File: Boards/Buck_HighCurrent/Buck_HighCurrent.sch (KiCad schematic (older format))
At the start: 25 parts, among them U1 TPS563231

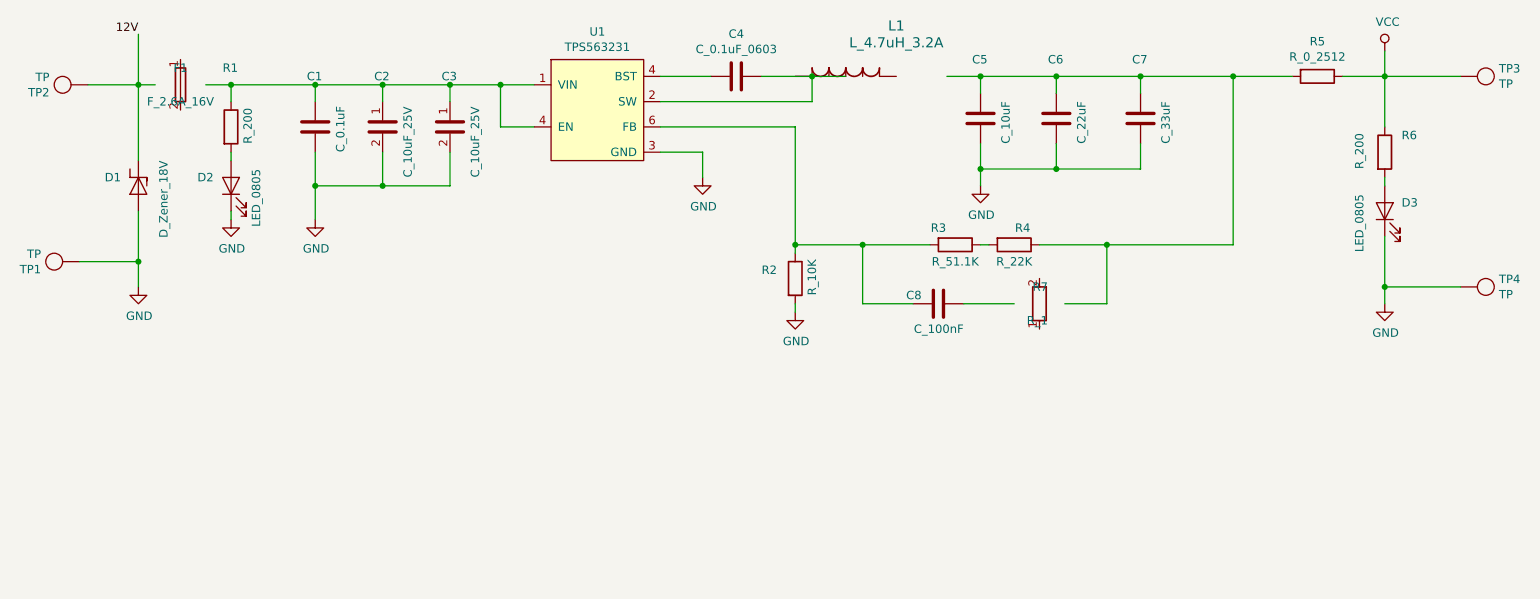
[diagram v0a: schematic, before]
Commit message: first pass layout with new buck.
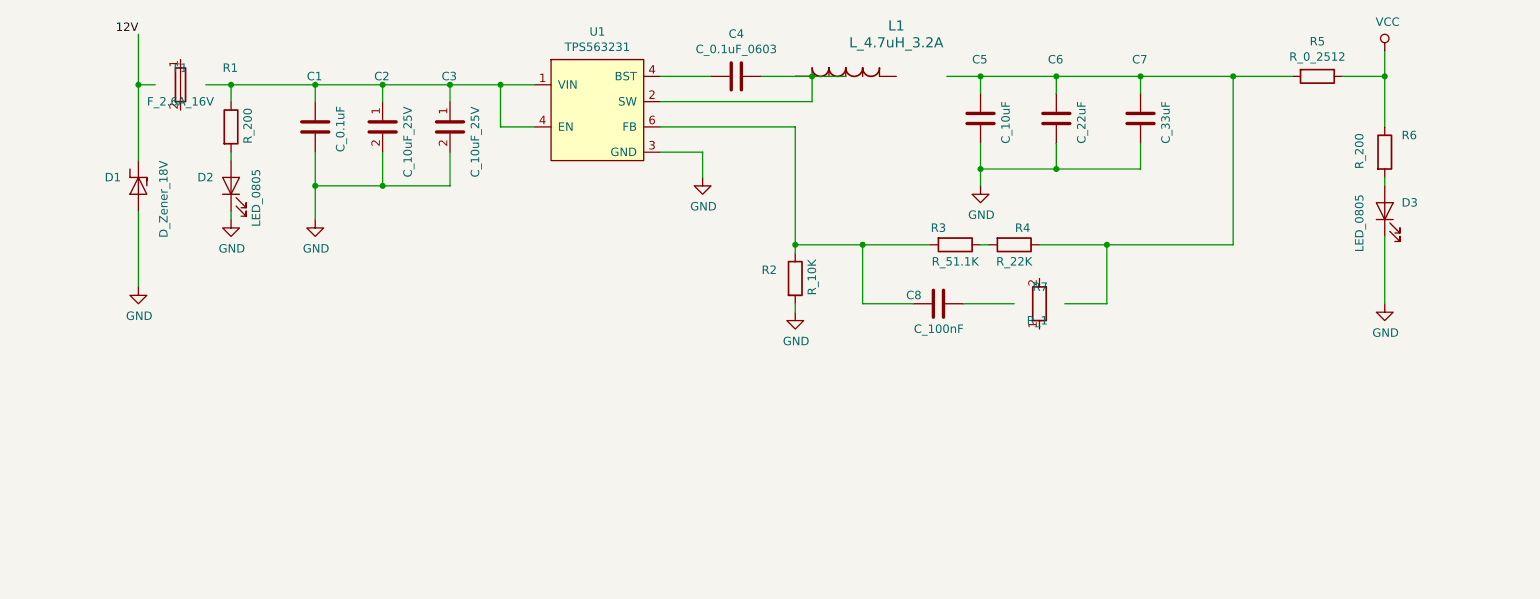
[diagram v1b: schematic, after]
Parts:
- removed TP1, TP2, TP3, TP4: TP, footprints:tp_1.6mm, symbol footprints:TP
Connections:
- wire segments 71 -> 65
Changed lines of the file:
@@
 	7300 3750 7000 3750
-$Comp
-L footprints:TP TP3
-U 1 1 5DDA5938
-P 10150 2400
-F 0 "TP3" V 10104 2428 50  0000 L CNN
-F 1 "TP" V 10195 2428 50  0000 L CNN
-F 2 "footprints:tp_1.6mm" H 10050 2300 50  0001 C CNN
-F 3 "http://www.keyelco.com/product-pdf.cfm?p=1314" H 10150 2400 50  0001 C CNN
-F 4 "DK" H 10250 2500 50  0001 C CNN "MFN"
-F 5 "36-5006-ND" H 10350 2600 50  0001 C CNN "MPN"
-F 6 "https://www.digikey.com/product-detail/en/keystone-electronics/5006/36-5006-ND/255330" H 10450 2700 50  0001 C CNN "PurchasingLink"
-	1    10150 2400
-	0    1    1    0
-$EndComp
-$Comp
-L footprints:TP TP4
-U 1 1 5DDA7C84
-P 10150 3650
-F 0 "TP4" V 10104 3678 50  0000 L CNN
-F 1 "TP" V 10195 3678 50  0000 L CNN
-F 2 "footprints:tp_1.6mm" H 10050 3550 50  0001 C CNN
-F 3 "http://www.keyelco.com/product-pdf.cfm?p=1314" H 10150 3650 50  0001 C CNN
-F 4 "DK" H 10250 3750 50  0001 C CNN "MFN"
-F 5 "36-5006-ND" H 10350 3850 50  0001 C CNN "MPN"
-F 6 "https://www.digikey.com/product-detail/en/keystone-electronics/5006/36-5006-ND/255330" H 10450 3950 50  0001 C CNN "PurchasingLink"
-	1    10150 3650
-	0    1    1    0
-$EndComp
-Wire Wire Line
-	9500 3350 9500 3650
-Wire Wire Line
-	9500 2400 9950 2400
-Wire Wire Line
-	9950 3650 9500 3650
-Connection ~ 9500 3650
-Wire Wire Line
-	9500 3650 9500 3750
-$Comp
-L footprints:TP TP1
-U 1 1 5DDB2371
-P 1550 3500
-F 0 "TP1" V 1504 3528 50  0000 L CNN
-F 1 "TP" V 1595 3528 50  0000 L CNN
-F 2 "footprints:tp_1.6mm" H 1450 3400 50  0001 C CNN
-F 3 "http://www.keyelco.com/product-pdf.cfm?p=1314" H 1550 3500 50  0001 C CNN
-F 4 "DK" H 1650 3600 50  0001 C CNN "MFN"
-F 5 "36-5006-ND" H 1750 3700 50  0001 C CNN "MPN"
-F 6 "https://www.digikey.com/product-detail/en/keystone-electronics/5006/36-5006-ND/255330" H 1850 3800 50  0001 C CNN "PurchasingLink"
-	1    1550 3500
-	0    -1   -1   0
-$EndComp
-Wire Wire Line
-	1750 3500 2100 3500
-Wire Wire Line
-	2100 3200 2100 3500
-Connection ~ 2100 3500
-Wire Wire Line
-	2100 3500 2100 3650
-$Comp
-L footprints:TP TP2
-U 1 1 5DDB56F7
-P 1600 2450
-F 0 "TP2" V 1554 2478 50  0000 L CNN
-F 1 "TP" V 1645 2478 50  0000 L CNN
-F 2 "footprints:tp_1.6mm" H 1500 2350 50  0001 C CNN
-F 3 "http://www.keyelco.com/product-pdf.cfm?p=1314" H 1600 2450 50  0001 C CNN
-F 4 "DK" H 1700 2550 50  0001 C CNN "MFN"
-F 5 "36-5006-ND" H 1800 2650 50  0001 C CNN "MPN"
-F 6 "https://www.digikey.com/product-detail/en/keystone-electronics/5006/36-5006-ND/255330" H 1900 2750 50  0001 C CNN "PurchasingLink"
-	1    1600 2450
-	0    -1   -1   0
-$EndComp
-Wire Wire Line
-	1800 2450 2100 2450
 $Comp
 L footprints:R_10K R2
@@
 Wire Wire Line
 	7850 3400 8600 3400
+Wire Wire Line
+	2100 3200 2100 3650
+Wire Wire Line
+	9500 3350 9500 3750
 $EndSCHEMATC

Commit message: 3A buck, rev2.0, no magic smoke now
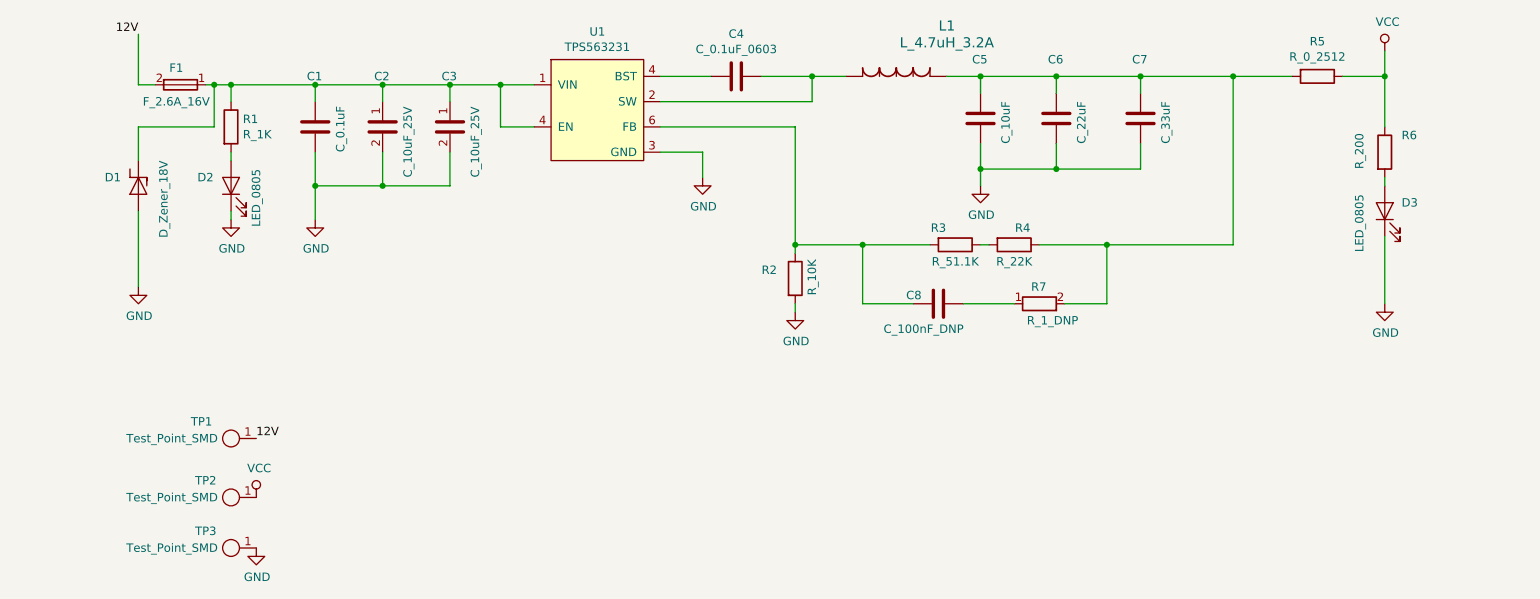
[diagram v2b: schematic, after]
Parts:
- removed R1: R_200, footprints:R_0805_OEM, symbol footprints:R_200
- added R1: R_1K, footprints:R_0805_OEM, symbol footprints:R_1K
- added TP1, TP2, TP3: Test_Point_SMD, footprints:Test_Point_SMD, symbol formula:Test_Point_SMD
- C8: value C_100nF -> C_100nF_DNP
- R7: value R_1 -> R_1_DNP
- U1: footprint footprints:SOT-563 -> Package_TO_SOT_SMD:SOT-563
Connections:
- wire segments 65 -> 68
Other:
- moved on the sheet: F1, L1, R7
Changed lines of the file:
@@
-$EndComp
-$Comp
-L footprints:R_200 R1
-U 1 1 5DD24939
-P 2650 2700
-F 0 "R1" H 2600 3050 50  0000 L CNN
-F 1 "R_200" V 2750 2600 50  0000 L CNN
-F 2 "footprints:R_0805_OEM" H 2580 2700 50  0001 C CNN
-F 3 "https://www.seielect.com/Catalog/SEI-RMCF_RMCP.pdf" H 2730 2700 50  0001 C CNN
-F 4 "DK" H 2650 2700 60  0001 C CNN "MFN"
-F 5 "RMCF0805JT200RCT-ND" H 2650 2700 60  0001 C CNN "MPN"
-F 6 "https://www.digikey.com/products/en?keywords=RMCF0805JT200RCT-ND" H 3130 3100 60  0001 C CNN "PurchasingLink"
-	1    2650 2700
-	1    0    0    -1
 $EndComp
 $Comp
@@
 	1    0    0    -1
 $EndComp
-Wire Wire Line
-	2100 2900 2100 2450
 $Comp
 L footprints:F_2.6A_16V F1
 U 1 1 5DD2DCBD
 P 2350 2450
-F 0 "F1" V 2250 2450 50  0000 C CNN
-F 1 "F_2.6A_16V" V 2450 2450 50  0000 C CNN
+F 0 "F1" H 2375 2350 50  0000 C CNN
+F 1 "F_2.6A_16V" H 2375 2550 50  0000 C CNN
 F 2 "Fuse:Fuse_1812_4532Metric" H 2350 2450 50  0001 C CNN
 F 3 "https://www.belfuse.com/resources/CircuitProtection/datasheets/0ZCG%20Nov2016.pdf" H 2350 2450 50  0001 C CNN
 F 4 "https://www.digikey.com/product-detail/en/bel-fuse-inc/0ZCG0260BF2B/507-1780-6-ND/4156287" H 2410 2359 50  0001 L CNN "Digikey"
 	1    2350 2450
-	0    1    1    0
+	-1   0    0    1
 $EndComp
 Wire Wire Line
@@
 Connection ~ 4250 2450
 Wire Wire Line
-	2500 2450 2650 2450
+	2500 2450 2550 2450
 Connection ~ 2650 2450
 Wire Wire Line
@@
 L footprints:IHLP2020BZER4R7M11 L1
 U 1 1 5DD494D5
-P 6300 2400
-F 0 "L1" H 6600 2700 60  0000 C CNN
-F 1 "L_4.7uH_3.2A" H 6600 2600 60  0000 C CNN
-F 2 "footprints:IHLP2020BZER4R7M11" H 6575 2115 60  0001 C CNN
-F 3 "http://www.vishay.com/docs/34261/ihlp2020bz11.pdf" H 6300 2400 60  0001 C CNN
-F 4 "https://www.digikey.com/product-detail/en/vishay-dale/IHLP2020BZER4R7M11/541-1222-1-ND/2025112" H 6300 2400 50  0001 C CNN "Vendor Link"
-	1    6300 2400
+P 6600 2400
+F 0 "L1" H 6900 2700 60  0000 C CNN
+F 1 "L_4.7uH_3.2A" H 6900 2600 60  0000 C CNN
+F 2 "footprints:IHLP2020BZER4R7M11" H 6875 2115 60  0001 C CNN
+F 3 "http://www.vishay.com/docs/34261/ihlp2020bz11.pdf" H 6600 2400 60  0001 C CNN
+F 4 "https://www.digikey.com/product-detail/en/vishay-dale/IHLP2020BZER4R7M11/541-1222-1-ND/2025112" H 6600 2400 50  0001 C CNN "Vendor Link"
+	1    6600 2400
 	1    0    0    -1
 $EndComp
@@
 Wire Wire Line
 	2100 2150 2100 2450
-Connection ~ 2100 2450
 Wire Wire Line
 	7450 3400 7850 3400
@@
 P 6850 3750
 F 0 "C8" V 6900 3850 50  0000 L CNN
-F 1 "C_100nF" V 6700 3600 50  0000 L CNN
+F 1 "C_100nF_DNP" V 6700 3600 50  0000 L CNN
 F 2 "footprints:C_0603_1608Metric" H 6888 3600 50  0001 C CNN
 F 3 "http://www.samsungsem.com/kr/support/product-search/mlcc/CL10A475KQ8NNNC.jsp" H 6875 3850 50  0001 C CNN
@@
 U 1 1 5DD86588
 P 7450 3750
-F 0 "R7" V 7550 3700 50  0000 L CNN
-F 1 "R_1" V 7350 3700 50  0000 L CNN
+F 0 "R7" H 7400 3850 50  0000 L CNN
+F 1 "R_1_DNP" H 7375 3650 50  0000 L CNN
 F 2 "footprints:R_0603_1608Metric" H 7450 3750 50  0001 C CNN
 F 3 "" H 7450 3750 50  0001 C CNN
 F 4 "https://www.digikey.com/product-detail/en/yageo/RC0603FR-071RL/311-1.00HRCT-ND/729789" H 7450 3750 50  0001 C CNN "Link"
 	1    7450 3750
-	0    -1   -1   0
+	1    0    0    -1
 $EndComp
 $Comp
@@
 F 0 "U1" H 4825 3665 50  0000 C CNN
 F 1 "TPS563231" H 4825 3574 50  0000 C CNN
-F 2 "footprints:SOT-563" H 4850 3050 50  0001 C CNN
+F 2 "Package_TO_SOT_SMD:SOT-563" H 4850 3050 50  0001 C CNN
 F 3 "" H 4850 3050 50  0001 C CNN
 	1    4850 2900
@@
 Wire Wire Line
 	9500 3350 9500 3750
+Wire Wire Line
+	2100 2900 2100 2700
+Wire Wire Line
+	2100 2700 2550 2700
+Wire Wire Line
+	2550 2700 2550 2450
+Connection ~ 2550 2450
+Wire Wire Line
+	2550 2450 2650 2450
+$Comp
+L formula:Test_Point_SMD TP1
+U 1 1 5E474401
+P 2750 4550
+F 0 "TP1" V 2850 4825 50  0000 C CNN
+F 1 "Test_Point_SMD" V 2750 5000 50  0000 C CNN
+F 2 "footprints:Test_Point_SMD" H 2750 4400 50  0001 C CNN
+F 3 "" H 2750 4550 50  0001 C CNN
+	1    2750 4550
+	0    -1   -1   0
+$EndComp
+$Comp
+L formula:Test_Point_SMD TP2
+U 1 1 5E475044
+P 2750 4900
+F 0 "TP2" V 2850 5150 50  0000 C CNN
+F 1 "Test_Point_SMD" V 2750 5350 50  0000 C CNN
+F 2 "footprints:Test_Point_SMD" H 2750 4750 50  0001 C CNN
+F 3 "" H 2750 4900 50  0001 C CNN
+	1    2750 4900
+	0    -1   -1   0
+$EndComp
+$Comp
+L formula:Test_Point_SMD TP3
+U 1 1 5E476704
+P 2750 5200
+F 0 "TP3" V 2850 5450 50  0000 C CNN
+F 1 "Test_Point_SMD" V 2750 5650 50  0000 C CNN
+F 2 "footprints:Test_Point_SMD" H 2750 5050 50  0001 C CNN
+F 3 "" H 2750 5200 50  0001 C CNN
+	1    2750 5200
+	0    -1   -1   0
+$EndComp
+Text Label 2800 4550 0    50   ~ 0
+12V
+$Comp
+L power:GND #PWR0109
+U 1 1 5E478F28
+P 2800 5200
+F 0 "#PWR0109" H 2800 4950 50  0001 C CNN
+F 1 "GND" H 2805 5027 50  0000 C CNN
+F 2 "" H 2800 5200 50  0001 C CNN
+F 3 "" H 2800 5200 50  0001 C CNN
+	1    2800 5200
+	1    0    0    -1
+$EndComp
+$Comp
+L power:VCC #PWR0110
+U 1 1 5E479993
+P 2800 4900
+F 0 "#PWR0110" H 2800 4750 50  0001 C CNN
+F 1 "VCC" H 2817 5073 50  0000 C CNN
+F 2 "" H 2800 4900 50  0001 C CNN
+F 3 "" H 2800 4900 50  0001 C CNN
+	1    2800 4900
+	1    0    0    -1
+$EndComp
+$Comp
+L footprints:R_1K R1
+U 1 1 5E47F47B
+P 2650 2700
+F 0 "R1" H 2720 2746 50  0000 L CNN
+F 1 "R_1K" H 2720 2655 50  0000 L CNN
+F 2 "footprints:R_0805_OEM" H 2580 2700 50  0001 C CNN
+F 3 "https://www.seielect.com/Catalog/SEI-rncp.pdf" H 2730 2700 50  0001 C CNN
+F 4 "DK" H 2650 2700 60  0001 C CNN "MFN"
+F 5 "RNCP0805FTD1K00CT-ND" H 2650 2700 60  0001 C CNN "MPN"
+F 6 "https://www.digikey.com/products/en?keywords=RNCP0805FTD1K00CT-ND" H 3130 3100 60  0001 C CNN "PurchasingLink"
+	1    2650 2700
+	1    0    0    -1
+$EndComp
 $EndSCHEMATC
